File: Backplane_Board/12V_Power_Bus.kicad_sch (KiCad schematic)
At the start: 17 parts

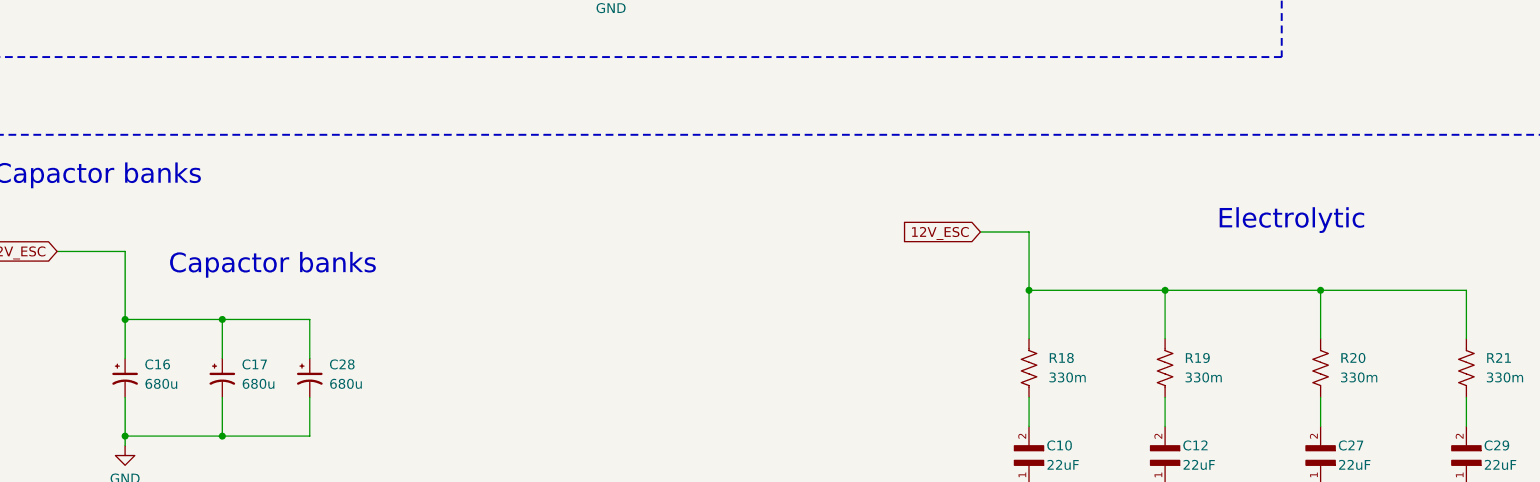
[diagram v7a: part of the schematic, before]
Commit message: added power swtching circits
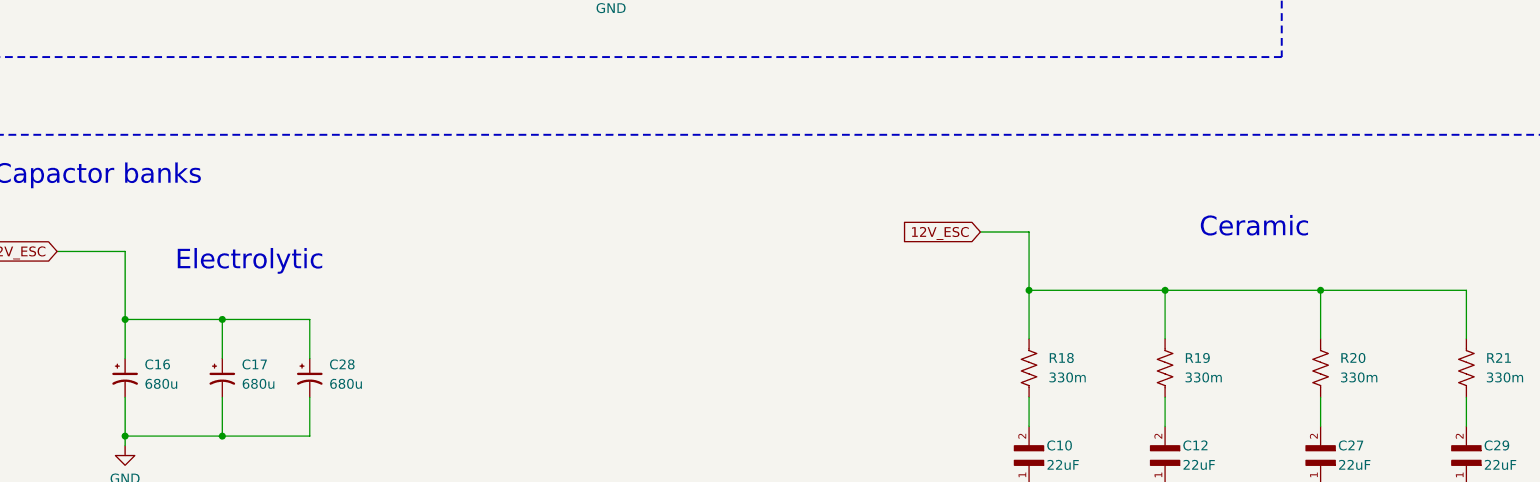
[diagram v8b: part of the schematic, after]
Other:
- note added: "Ceramic"
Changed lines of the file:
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@@
 		)
 	)
-	(text "Capactor banks"
+	(text "Ceramic"
 		(exclude_from_sim no)
-		(at 90.424 112.268 0)
+		(at 218.694 107.442 0)
 		(effects
 			(font
@@
 	(text "Electrolytic"
 		(exclude_from_sim no)
-		(at 223.52 106.426 0)
+		(at 87.376 111.76 0)
 		(effects
 			(font
